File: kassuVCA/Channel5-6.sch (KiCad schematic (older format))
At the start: 65 parts, among them Q401 MMBT3904, Q402 MBT3904DW1, Q403 MBT3904DW1, Q404 MMBT3904, SW401 mute5, SW402 SW_DPDT_x2, U401 TL072, U402 TL072

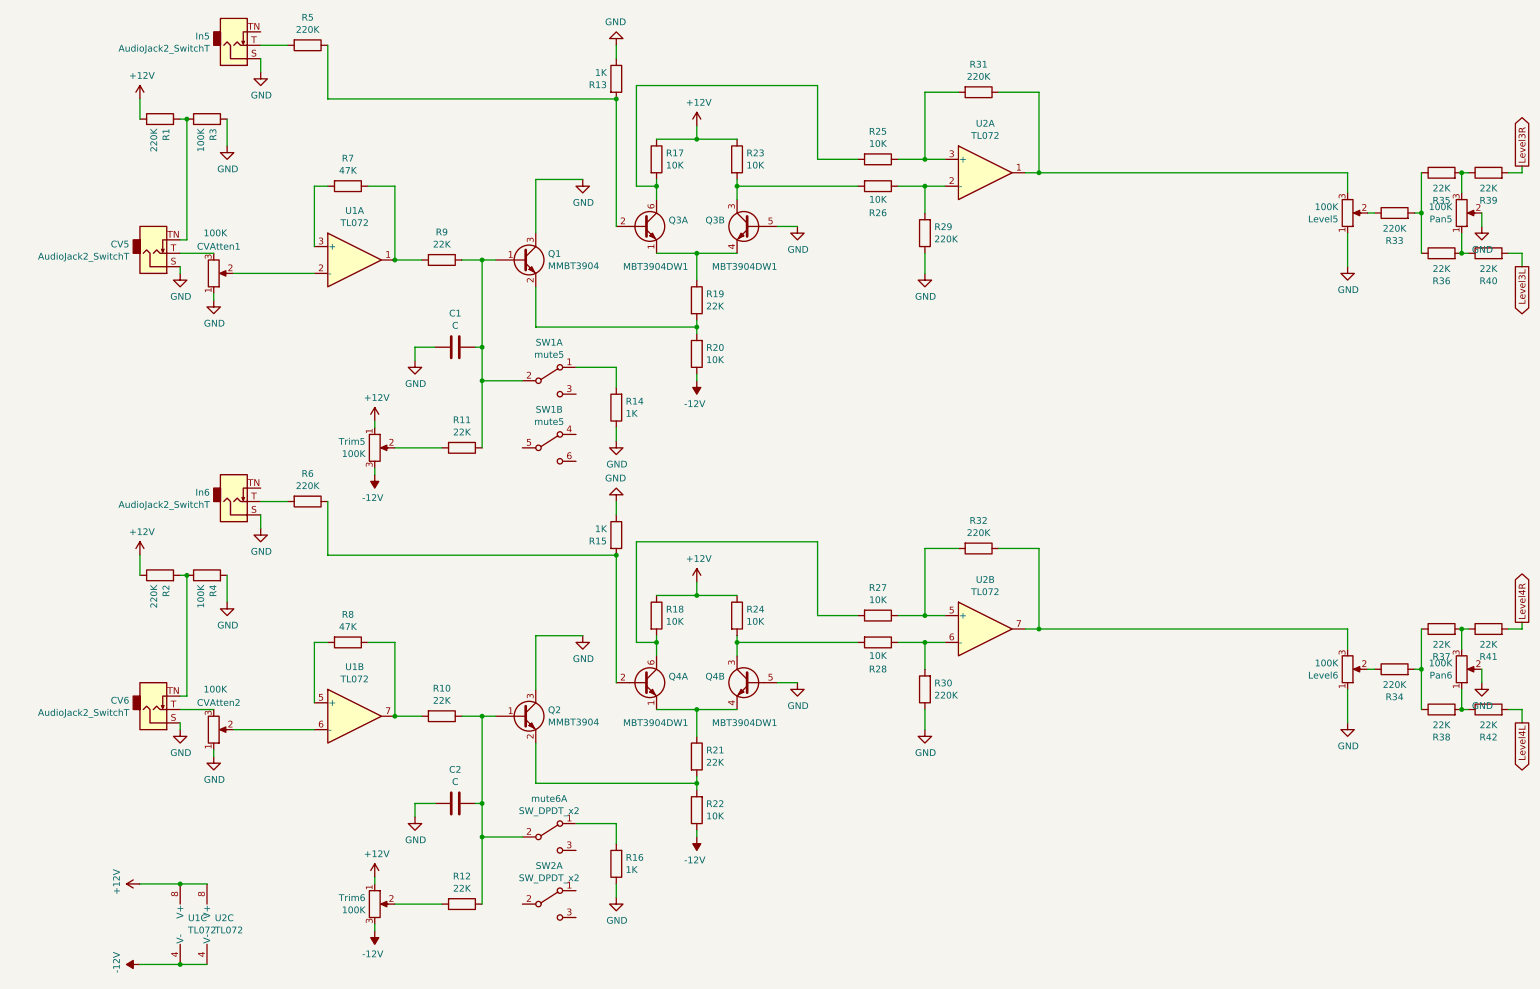
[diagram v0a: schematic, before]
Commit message: mixer WIP, 8 channels, more or less
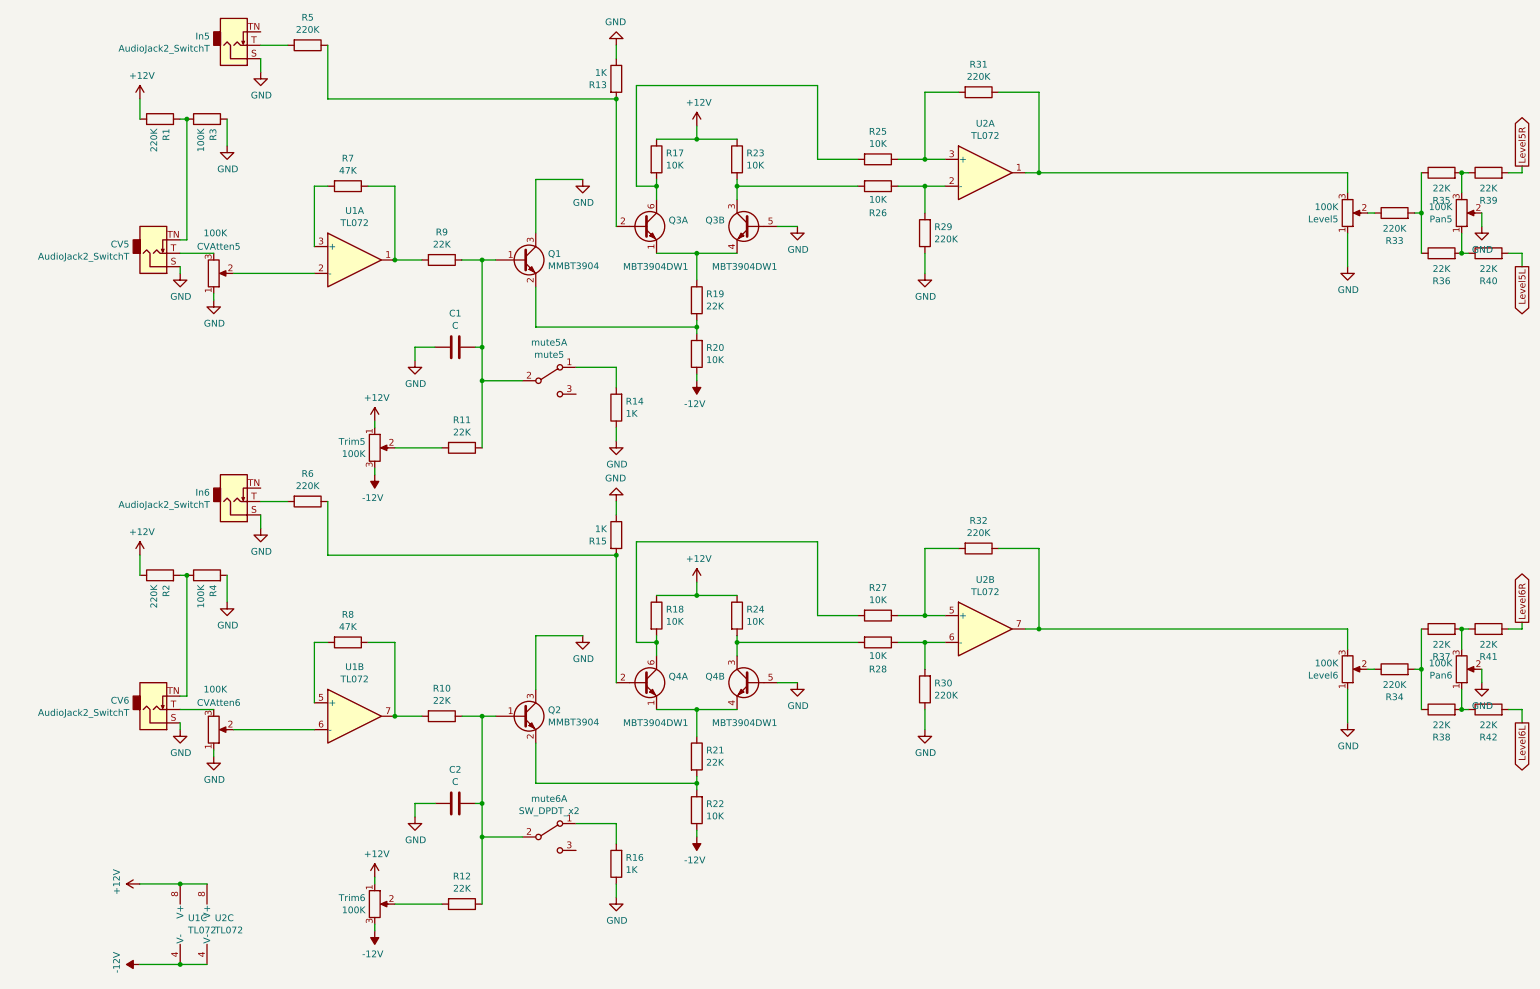
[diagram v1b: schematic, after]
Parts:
- removed unit 2 of SW401
- removed SW402 (x2): SW_DPDT_x2, MixerFootprints:A-330-6mm-dpdt, symbol Switch:SW_DPDT_x2
- added SW402: SW_DPDT_x2, MixerFootprints:A-330-6mm-dpdt, symbol Switch:SW_DPDT_x2
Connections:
- net at C402.1, Q404.1 (B), R410.1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: now also SW402.2 (B)
- net at R416.2: now also SW402.1 (A)
- net Level3L renamed Level5L
- net Level3R renamed Level5R
- net Level4L renamed Level6L
- net Level4R renamed Level6R
